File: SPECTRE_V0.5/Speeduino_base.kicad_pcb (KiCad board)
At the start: 2 copper layers, 100 x 93 mm, 209 parts, among them J1 Conn_01x04_Male, J2 Conn_02x04_Odd_Even, J3 Conn_01x06_Male, Q1 2N7002, Q10 BSP78, Q11 BSP78, Q12 BSP78, Q13 BSP78, Q14 BSP78, Q15 BSP78, Q16 SMD-MOSFET-N-CH-55V-2.1A-AO34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, Q17 AO3401A, Q18 BSP78, Q19 SMD-MOSFET-N-CH-55V-2.1A-AO34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, Q2 CJ2302, Q20 AO3401A, Q21 SMD-MOSFET-N-CH-55V-2.1A-AO34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, Q22 SMD-MOSFET-N-CH-55V-2.1A-AO34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, Q23 AO3401A, Q24 AO3401A, Q25 BSP78, Q26 BSP78, Q3 CJ2302, Q4 CJ2302, Q5 BSP78, Q6 BSP78, Q7 CJ2302, Q8 CJ2302, Q9 CJ2302, U1 MAX9926UAEE+, U2 molex_48pin, U3 LM78M05_TO220, U4 MAX3232

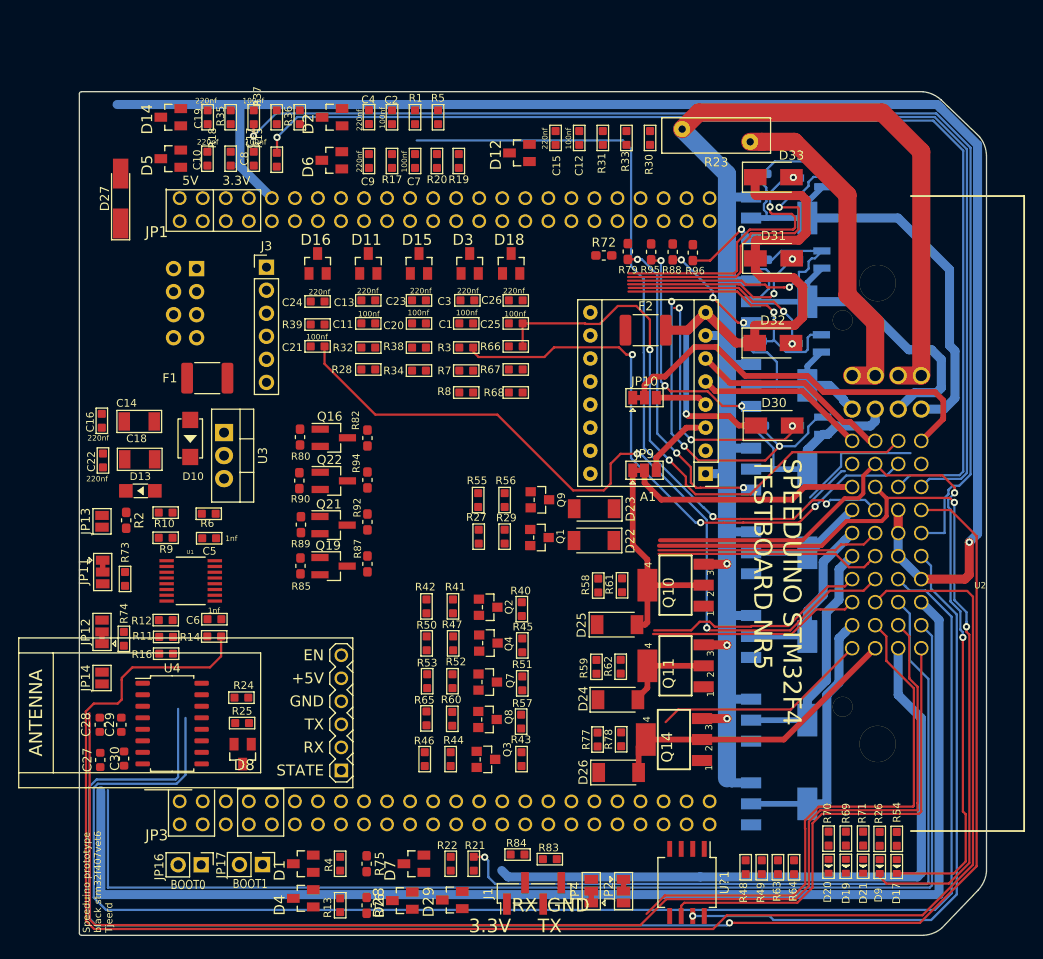
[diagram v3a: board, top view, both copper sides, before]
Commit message: Updates on routing V0.5 board
Switched some pins also updated the board routing a bit. not done yet.
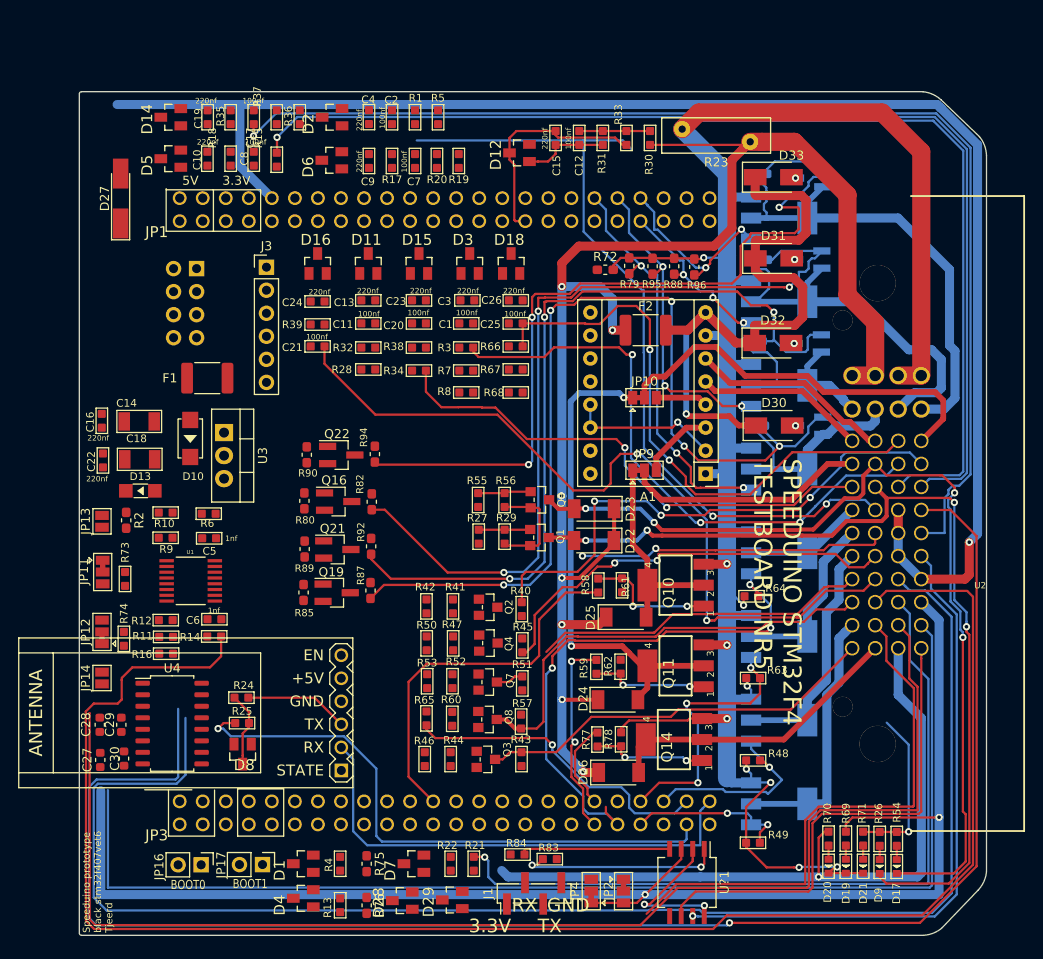
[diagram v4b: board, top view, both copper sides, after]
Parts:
- moved R64 30.2 mm to (188.1, 72.6), turned to 270 degrees
- moved R63 21.0 mm to (188.3, 81.6), turned to 270 degrees
- moved R48 11.8 mm to (188.3, 90.7), turned to 270 degrees
- moved R82 7.05 mm to (146.2, 62.2)
- moved Q16 7.05 mm to (142.5, 62.2)
- moved R80 7.05 mm to (138.8, 62.1)
- moved Q22 2.97 mm to (142.9, 57.0)
- moved R90 2.97 mm to (139.1, 57.0)
- moved R94 2.97 mm to (146.6, 57.0)
- moved Q19 2.95 mm to (142.4, 72.2)
- moved R85 2.95 mm to (138.7, 72.2)
- moved R87 2.95 mm to (146.1, 72.0)
- moved R49 2.86 mm to (188.3, 99.8), turned to 270 degrees
- moved R89 2.72 mm to (138.8, 67.4)
- moved Q21 2.72 mm to (142.4, 67.5)
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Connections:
- Q18 pad 1: PE13 -> PE14
- Q26 pad 1: PE14 -> PE13
- R59 pad 1: PC8 -> PC7
- R77 pad 1: PC7 -> PC8
- R88 pad 1: PE13 -> PE14
- R96 pad 1: PE14 -> PE13
- U2 pad 13: IGN4-OUT -> IGN1-OUT
- U2 pad 16: IGN1-OUT -> Net-(JP9-Pad2)
- U2 pad 20: Net-(JP9-Pad2) -> CLT_2
- U2 pad 27: CLT_2 -> CLT
- U2 pad 31: CLT -> IGN2-OUT
- U2 pad 36: IGN2-OUT -> IGN3-OUT
- U2 pad 40: IGN3-OUT -> IGN4-OUT
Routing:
- net VBAT: track 36.9 -> 187.1 mm, vias 0 -> 8
- net PWR_GND: track 164.6 -> 234.7 mm, vias 3 -> 10
- net PD9: track 0.00 -> 65.0 mm, vias 0 -> 1
- net Net-(Q20-Pad1): track 37.8 -> 101.3 mm, vias 3 -> 5
- net Net-(Q17-Pad1): track 30.6 -> 91.2 mm, vias 1 -> 3
- net PD15: track 0.00 -> 59.8 mm, vias 0 -> 3
- net Net-(Q23-Pad1): track 28.7 -> 88.4 mm, vias 1 -> 3
- net PD8: track 0.00 -> 53.9 mm
- net Net-(Q24-Pad1): track 42.3 -> 89.6 mm, vias 1 -> 3
- net IGN1-OUT: track 14.0 -> 58.4 mm, vias 0 -> 3
- net IGN4-OUT: track 5.43 -> 49.4 mm
- net IDLE1-OUT: track 10.6 -> 54.3 mm, vias 0 -> 2
- net PD3: track 0.00 -> 41.6 mm
- net PD10: track 0.00 -> 34.7 mm, vias 0 -> 1
- net CLT_2: track 24.7 -> 56.7 mm, vias 0 -> 2
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
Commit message: Routing and testing
Test Some more functions of the V0.3 also routed the V0.5 furhter
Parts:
- moved R83 4.04 mm to (169.9, 101.5), turned to 90 degrees
- moved D1 0.60 mm to (138.1, 102.1)
- moved D4 0.59 mm to (138.1, 106.0)
- moved J1 0.47 mm to (164.1, 105.8)
- moved R84 0.40 mm to (162.5, 101.5)
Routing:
- net 3.3V: track 95.1 -> 250.3 mm, vias 2 -> 9
- net PWR_GND: track 234.7 -> 344.3 mm, vias 10 -> 22
- net GND: track 196.6 -> 293.9 mm, vias 3 -> 4
- net VR1+: track 60.2 -> 141.3 mm
- net Net-(D1-Pad3): track 0.00 -> 57.6 mm, vias 0 -> 3
- net VBAT_F1: track 0.00 -> 48.0 mm, vias 0 -> 1
- net Net-(JP4-Pad2): track 0.00 -> 38.7 mm, vias 0 -> 5
- net PB9: track 0.00 -> 34.2 mm
- net PA8: track 0.00 -> 29.4 mm
- net VBAT: track 187.1 -> 214.2 mm, vias 8 -> 9
- net Net-(JP2-Pad2): track 0.00 -> 24.5 mm, vias 0 -> 2
- net Net-(D4-Pad3): track 0.00 -> 23.0 mm
- net PD7: track 0.00 -> 22.5 mm
- net PD0: track 0.00 -> 22.0 mm
- net PE1: track 0.00 -> 19.4 mm
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
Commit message: Somem ore routing V0.5
Routing board V0.5
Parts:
- added JP5: Jumper_NC_Small, Jumper:SolderJumper-2_P1.3mm_Bridged_Pad1.0x1.5mm, F.Cu at (188.6, 106.5)
- added R97: 120, Speeduino_base:R0603, F.Cu at (192.0, 106.7)
- moved R23 1.18 mm to (180.4, 22.3)
- moved C24 0.18 mm to (140.2, 40.0), turned to 90 degrees
- turned R34 to 90 degrees
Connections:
- JP4 pad 3: Net-(JP4-Pad3) -> VBAT_F1
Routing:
- net GND: track 293.9 -> 427.0 mm, vias 4 -> 9
- net 3.3V: track 250.3 -> 363.2 mm, vias 9 -> 14
- net 5V: track 164.1 -> 276.6 mm
- net PE8: track 0.00 -> 66.4 mm, vias 0 -> 2
- net PE12: track 0.00 -> 61.8 mm, vias 0 -> 1
- net VBAT_F1: track 48.0 -> 103.2 mm, vias 1 -> 2
- net PE10: track 0.00 -> 52.8 mm, vias 0 -> 1
- net VBAT: track 214.2 -> 259.5 mm, vias 9 -> 11
- net PE15: track 0.00 -> 43.9 mm
- net PE7: track 0.00 -> 38.9 mm, vias 0 -> 3
- net PC13: track 0.00 -> 35.8 mm, vias 0 -> 2
- net IAT_2: track 74.7 -> 110.4 mm, vias 0 -> 1
- net PE5: track 0.00 -> 34.6 mm, vias 0 -> 1
- net PC4: track 0.00 -> 29.2 mm, vias 0 -> 1
- net PD8: track 62.2 -> 77.8 mm, vias 0 -> 1
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
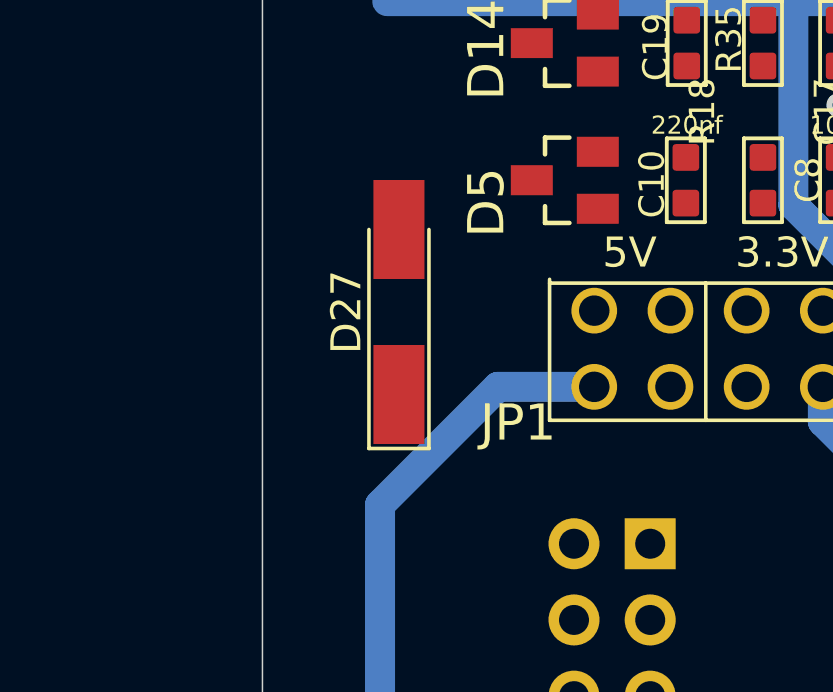
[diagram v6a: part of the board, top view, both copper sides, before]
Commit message: 3.3V power protection
Extra protection for the 3.3volt supply. TL431 is used for this.
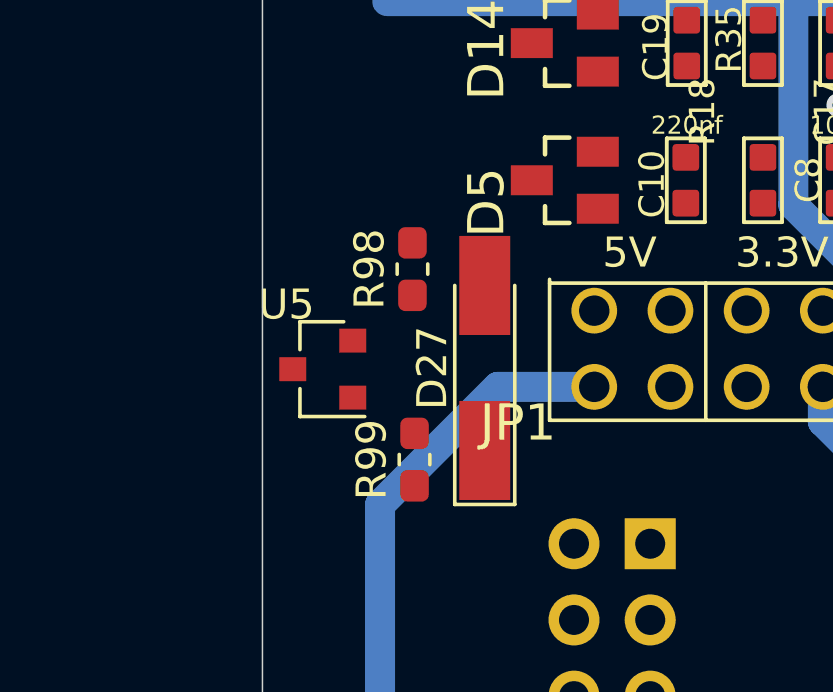
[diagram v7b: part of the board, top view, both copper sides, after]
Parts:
- added R98: 2k49, Resistor_SMD:R_0603_1608Metric_Pad1.05x0.95mm_HandSolder, F.Cu at (119.0, 27.3)
- added R99: 1k8, Resistor_SMD:R_0603_1608Metric_Pad1.05x0.95mm_HandSolder, F.Cu at (119.1, 33.7)
- added U5: TL431DBZ, Package_TO_SOT_SMD:SOT-23, F.Cu at (116.0, 30.7)
- moved D27 3.41 mm to (121.4, 30.6)
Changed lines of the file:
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@@
     (tracks 2085)
     (zones 0)
-    (modules 211)
-    (nets 208)
+    (modules 214)
+    (nets 209)
   )
   (page A4)
@@
   (net 206 "Net-(Q24-Pad1)")
   (net 207 "Net-(JP5-Pad2)")
+  (net 208 "Net-(R98-Pad1)")
   (net_class Default "This is the default net class."
     (clearance 0.15)
@@
     (add_net "Net-(Q9-Pad1)")
     (add_net "Net-(R84-Pad2)")
+    (add_net "Net-(R98-Pad1)")
     (add_net "Net-(U$2-Pad1)")
     (add_net "Net-(U$2-Pad6)")
@@
     (add_net V_IDLE)
   )
+  (module Package_TO_SOT_SMD:SOT-23 (layer Top)
+    (at 116.01 30.68 180)
+    (descr "SOT-23, Standard")
+    (tags SOT-23)
+    (attr smd)
+    (fp_text reference U5 (at 1.21 2.15) (layer F.SilkS)
+      (effects (font (size 1 1) (thickness 0.15)))
+    )
+    (fp_text value TL431DBZ (at 0 2.5) (layer F.Fab)
+      (effects (font (size 1 1) (thickness 0.15)))
+    )
+    (fp_line (start 0.76 1.58) (end -0.7 1.58) (layer F.SilkS) (width 0.12))
+    (fp_line (start 0.76 -1.58) (end -1.4 -1.58) (layer F.SilkS) (width 0.12))
+    (fp_line (start -1.7 1.75) (end -1.7 -1.75) (layer F.CrtYd) (width 0.05))
+    (fp_line (start 1.7 1.75) (end -1.7 1.75) (layer F.CrtYd) (width 0.05))
+    (fp_line (start 1.7 -1.75) (end 1.7 1.75) (layer F.CrtYd) (width 0.05))
+    (fp_line (start -1.7 -1.75) (end 1.7 -1.75) (layer F.CrtYd) (width 0.05))
+    (fp_line (start 0.76 -1.58) (end 0.76 -0.65) (layer F.SilkS) (width 0.12))
+    (fp_line (start 0.76 1.58) (end 0.76 0.65) (layer F.SilkS) (width 0.12))
+    (fp_line (start -0.7 1.52) (end 0.7 1.52) (layer F.Fab) (width 0.1))
+    (fp_line (start 0.7 -1.52) (end 0.7 1.52) (layer F.Fab) (width 0.1))
+    (fp_line (start -0.7 -0.95) (end -0.15 -1.52) (layer F.Fab) (width 0.1))
+    (fp_line (start -0.15 -1.52) (end 0.7 -1.52) (layer F.Fab) (width 0.1))
+    (fp_line (start -0.7 -0.95) (end -0.7 1.5) (layer F.Fab) (width 0.1))
+    (fp_text user %R (at 0 0 90) (layer F.Fab)
+      (effects (font (size 0.5 0.5) (thickness 0.075)))
+    )
+    (pad 3 smd rect (at 1 0 180) (size 0.9 0.8) (layers Top F.Paste F.Mask)
+      (net 1 GND))
+    (pad 2 smd rect (at -1 0.95 180) (size 0.9 0.8) (layers Top F.Paste F.Mask)
+      (net 208 "Net-(R98-Pad1)"))
+    (pad 1 smd rect (at -1 -0.95 180) (size 0.9 0.8) (layers Top F.Paste F.Mask)
+      (net 66 3.3V))
+    (model ${KISYS3DMOD}/Package_TO_SOT_SMD.3dshapes/SOT-23.wrl
+      (at (xyz 0 0 0))
+      (scale (xyz 1 1 1))
+      (rotate (xyz 0 0 0))
+    )
+  )
+  (module Resistor_SMD:R_0603_1608Metric_Pad1.05x0.95mm_HandSolder (layer Top)
+    (at 119.07 33.695 90)
+    (descr "Resistor SMD 0603 (1608 Metric), square (rectangular) end terminal, IPC_7351 nominal with elongated pad for handsoldering. (Body size source: http://www.tortai-tech.com/upload/download/2011102023233369053.pdf), generated with kicad-footprint-generator")
+    (tags "resistor handsolder")
+    (attr smd)
+    (fp_text reference R99 (at 0 -1.43 90) (layer F.SilkS)
+      (effects (font (size 1 1) (thickness 0.15)))
+    )
+    (fp_text value 1k8 (at 0 1.43 90) (layer F.Fab)
+      (effects (font (size 1 1) (thickness 0.15)))
+    )
+    (fp_text user %R (at 0 0 90) (layer F.Fab)
+      (effects (font (size 0.4 0.4) (thickness 0.06)))
+    )
+    (fp_line (start 1.65 0.73) (end -1.65 0.73) (layer F.CrtYd) (width 0.05))
+    (fp_line (start 1.65 -0.73) (end 1.65 0.73) (layer F.CrtYd) (width 0.05))
+    (fp_line (start -1.65 -0.73) (end 1.65 -0.73) (layer F.CrtYd) (width 0.05))
+    (fp_line (start -1.65 0.73) (end -1.65 -0.73) (layer F.CrtYd) (width 0.05))
+    (fp_line (start -0.171267 0.51) (end 0.171267 0.51) (layer F.SilkS) (width 0.12))
+    (fp_line (start -0.171267 -0.51) (end 0.171267 -0.51) (layer F.SilkS) (width 0.12))
+    (fp_line (start 0.8 0.4) (end -0.8 0.4) (layer F.Fab) (width 0.1))
+    (fp_line (start 0.8 -0.4) (end 0.8 0.4) (layer F.Fab) (width 0.1))
+    (fp_line (start -0.8 -0.4) (end 0.8 -0.4) (layer F.Fab) (width 0.1))
+    (fp_line (start -0.8 0.4) (end -0.8 -0.4) (layer F.Fab) (width 0.1))
+    (pad 2 smd roundrect (at 0.875 0 90) (size 1.05 0.95) (layers Top F.Paste F.Mask) (roundrect_rratio 0.25)
+      (net 208 "Net-(R98-Pad1)"))
+    (pad 1 smd roundrect (at -0.875 0 90) (size 1.05 0.95) (layers Top F.Paste F.Mask) (roundrect_rratio 0.25)
+      (net 66 3.3V))
+    (model ${KISYS3DMOD}/Resistor_SMD.3dshapes/R_0603_1608Metric.wrl
+      (at (xyz 0 0 0))
+      (scale (xyz 1 1 1))
+      (rotate (xyz 0 0 0))
+    )
+  )
+  (module Resistor_SMD:R_0603_1608Metric_Pad1.05x0.95mm_HandSolder (layer Top)
+    (at 119 27.345 90)
+    (descr "Resistor SMD 0603 (1608 Metric), square (rectangular) end terminal, IPC_7351 nominal with elongated pad for handsoldering. (Body size source: http://www.tortai-tech.com/upload/download/2011102023233369053.pdf), generated with kicad-footprint-generator")
+    (tags "resistor handsolder")
+    (attr smd)
+    (fp_text reference R98 (at 0 -1.43 90) (layer F.SilkS)
+      (effects (font (size 1 1) (thickness 0.15)))
+    )
+    (fp_text value 2k49 (at 0 1.43 90) (layer F.Fab)
+      (effects (font (size 1 1) (thickness 0.15)))
+    )
+    (fp_text user %R (at 0 0 90) (layer F.Fab)
+      (effects (font (size 0.4 0.4) (thickness 0.06)))
+    )
+    (fp_line (start 1.65 0.73) (end -1.65 0.73) (layer F.CrtYd) (width 0.05))
+    (fp_line (start 1.65 -0.73) (end 1.65 0.73) (layer F.CrtYd) (width 0.05))
+    (fp_line (start -1.65 -0.73) (end 1.65 -0.73) (layer F.CrtYd) (width 0.05))
+    (fp_line (start -1.65 0.73) (end -1.65 -0.73) (layer F.CrtYd) (width 0.05))
+    (fp_line (start -0.171267 0.51) (end 0.171267 0.51) (layer F.SilkS) (width 0.12))
+    (fp_line (start -0.171267 -0.51) (end 0.171267 -0.51) (layer F.SilkS) (width 0.12))
+    (fp_line (start 0.8 0.4) (end -0.8 0.4) (layer F.Fab) (width 0.1))
+    (fp_line (start 0.8 -0.4) (end 0.8 0.4) (layer F.Fab) (width 0.1))
+    (fp_line (start -0.8 -0.4) (end 0.8 -0.4) (layer F.Fab) (width 0.1))
+    (fp_line (start -0.8 0.4) (end -0.8 -0.4) (layer F.Fab) (width 0.1))
+    (pad 2 smd roundrect (at 0.875 0 90) (size 1.05 0.95) (layers Top F.Paste F.Mask) (roundrect_rratio 0.25)
+      (net 1 GND))
+    (pad 1 smd roundrect (at -0.875 0 90) (size 1.05 0.95) (layers Top F.Paste F.Mask) (roundrect_rratio 0.25)
+      (net 208 "Net-(R98-Pad1)"))
+    (model ${KISYS3DMOD}/Resistor_SMD.3dshapes/R_0603_1608Metric.wrl
+      (at (xyz 0 0 0))
+      (scale (xyz 1 1 1))
+      (rotate (xyz 0 0 0))
+    )
+  )
   (module Speeduino_base:R0603 (layer Top)
     (at 191.978 106.67 90)
@@
   )
   (module Diode_SMD:D_MiniMELF_Handsoldering (layer Top)
-    (at 118.55 28.775 90)
+    (at 121.41 30.64 90)
     (descr "Diode Mini-MELF Handsoldering")
     (tags "Diode Mini-MELF Handsoldering")

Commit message: routing V0.5
Some more routing V0.5
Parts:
- moved R68 7.74 mm to (162.0, 42.4)
- moved R67 7.62 mm to (161.9, 40.0)
- moved C26 5.37 mm to (161.8, 45.4)
- moved R3 5.37 mm to (156.7, 50.6)
- moved C25 5.31 mm to (161.8, 47.8)
- moved R7 5.30 mm to (156.8, 42.5), turned to 90 degrees
- moved C1 5.28 mm to (156.7, 47.8)
- moved R66 5.09 mm to (161.7, 50.1)
- moved R19 5.04 mm to (150.8, 24.6)
- moved R8 4.93 mm to (156.7, 45.2)
- moved C7 4.88 mm to (155.9, 24.6)
- turned C13 to 90 degrees
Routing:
- net GND: track 427.0 -> 549.9 mm, vias 9 -> 14
- net 3.3V: track 363.2 -> 484.0 mm, vias 14 -> 19
- net PE3: track 0.00 -> 51.5 mm, vias 0 -> 3
- net PE6: track 0.00 -> 46.3 mm, vias 0 -> 3
- net PE2: track 8.06 -> 47.2 mm, vias 0 -> 1
- net CLT: track 49.6 -> 80.5 mm, vias 2 -> 4
- net PC0: track 0.00 -> 29.1 mm, vias 0 -> 1
- net PC2: track 0.00 -> 28.6 mm, vias 0 -> 2
- net PA2: track 0.00 -> 23.9 mm, vias 0 -> 1
- net PC3: track 4.96 -> 18.4 mm
- net Net-(C3-Pad2): track 0.00 -> 12.3 mm
- net Net-(C26-Pad2): track 0.00 -> 11.6 mm
- net PA3: track 4.79 -> 16.2 mm
- net Net-(C19-Pad2): track 0.00 -> 11.0 mm
- net PC13: track 35.8 -> 45.5 mm, vias 2 -> 3
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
